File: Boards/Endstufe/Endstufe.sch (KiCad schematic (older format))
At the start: 56 parts, among them K1 DIP 7212-D, P1 CONN_3, P2 Trafo, P3 Relais, P4 6V3_AC, P5 Trafo_GK, P6 6V3_DC, P7 VSup1, P8 Bias, P9 CONN_5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

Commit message: Work in Progress
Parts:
- removed K1: DIP 7212-D, Reed:REED, symbol DIP~7212-D
- removed P1: CONN_3, MiniUniversalMate-N-LokSockets_13Aug2012:MiniUniversalMate-N-LokSocket_3PinVertical_12Aug2012, symbol CONN_3
- removed P3: Relais, w_conn_kk156:kk156_26-60-4020, symbol CONN_2
- removed P9: CONN_5, symbol CONN_5
- removed R24: 30k, Resistors_ThroughHole:Resistor_Horizontal_RM10mm, symbol R
- added J1: HV In, Connector_TE-Connectivity:TE_MATE-N-LOK_1-770875-x_2x03_P4.14mm_Vertical, symbol Endstufe-rescue:Conn_01x06
- added J2: Relais, Connector_Molex:Molex_KK-254_AE-6410-02A_1x02_P2.54mm_Vertical, symbol Endstufe-rescue:Conn_01x02
- added J3: NF_In, Connector_Molex:Molex_KK-254_AE-6410-02A_1x02_P2.54mm_Vertical, symbol Endstufe-rescue:Conn_01x02
- added K1: G6E, Relay_THT:Relay_SPDT_Omron_G6E, symbol Endstufe-rescue:G6E
- C1, C12, C13, C5: footprint Capacitors_ThroughHole:C_Disc_D7.5_P5 -> Capacitor_THT:C_Disc_D7.5mm_W4.4mm_P5.00mm; symbol C -> Endstufe-rescue:C
- C10, C11, C2, C3, C4, C8: footprint Capacitors_ThroughHole:C_Axial_D8_L21_P28 -> Capacitor_THT:C_Axial_L22.0mm_D9.5mm_P27.50mm_Horizontal; symbol C -> Endstufe-rescue:C
- C14, C15: footprint Capacitors_ThroughHole:C_Radial_D6.3_L11.2_P2.5 -> Capacitor_THT:CP_Radial_D6.3mm_P2.50mm; symbol C_Small -> Endstufe-rescue:C_Small
- C6: footprint Capacitors_ThroughHole:C_Disc_D6_P5 -> Capacitor_THT:C_Disc_D6.0mm_W2.5mm_P5.00mm; symbol C -> Endstufe-rescue:C
- C7: footprint Capacitors_ThroughHole:C_Disc_D3_P2.5 -> Capacitor_THT:C_Disc_D3.0mm_W2.0mm_P2.50mm; symbol C -> Endstufe-rescue:C
- C9: footprint Capacitors_ThroughHole:C_Disc_D7.5_P5 -> Capacitor_THT:C_Disc_D7.5mm_W2.5mm_P5.00mm; symbol C -> Endstufe-rescue:C
- P2: footprint Sockets_WAGO734:WAGO_734_5pin_Straight -> TerminalBlock_RND:TerminalBlock_RND_205-00004_1x05_P5.00mm_Horizontal; symbol CONN_5 -> Endstufe-rescue:CONN_5
- P4, P5, P6, P7: footprint Sockets_Mini-Universal:MiniUniversalMate-N-LokSocket_2PinVertical -> Connector_TE-Connectivity:TE_MATE-N-LOK_1-770866-x_1x02_P4.14mm_Vertical; symbol CONN_2 -> Endstufe-rescue:CONN_2
- P8: footprint Pin_Headers:Pin_Header_Straight_2x03_Pitch2.54mm -> Connector_PinHeader_2.54mm:PinHeader_2x03_P2.54mm_Vertical; symbol CONN_01X06 -> Endstufe-rescue:CONN_01X06
- R1, R11, R14, R15, R17, R18, R19, R2, R21, R22, R3, R6, R7, R8, R9: footprint Resistors_ThroughHole:Resistor_Horizontal_RM10mm -> Resistor_THT:R_Axial_DIN0207_L6.3mm_D2.5mm_P10.16mm_Horizontal; symbol R -> Endstufe-rescue:R
- R10, R13, R20, R23, R5: footprint Resistors_ThroughHole:Resistor_Ceramic_Horizontal_L23mm-W9mm-H9mm-p30mm -> Resistor_THT:R_Axial_Power_L25.0mm_W9.0mm_P30.48mm; symbol R -> Endstufe-rescue:R
- R12, R4: footprint Resistors_ThroughHole:Resistor_Horizontal_RM15mm -> Resistor_THT:R_Axial_DIN0207_L6.3mm_D2.5mm_P15.24mm_Horizontal; symbol R -> Endstufe-rescue:R
- R16: footprint Resistors_ThroughHole:Resistor_Horizontal_RM15mm -> Resistor_THT:R_Axial_DIN0207_L6.3mm_D2.5mm_P10.16mm_Horizontal; symbol R -> Endstufe-rescue:R
- RV2, RV3, RV5: footprint w_pth_resistors:trimmer_piher_pt10xv10 -> Potentiometer_THT:Potentiometer_Piher_PT-10-V10_Vertical; symbol POT-RESCUE-Endstufe -> Endstufe-rescue:POT-RESCUE-Endstufe
- T1, T2: footprint Valves:VALVE-OCTAL -> Valve:Valve_Octal; symbol KT88 -> Endstufe-rescue:KT88
- U1, U2: footprint Valves:VALVE-ECC-83-1 -> Valve:Valve_ECC-83-1; symbol ECC83 -> Endstufe-rescue:ECC83
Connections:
- net labels removed: 6V3
- wire segments 158 -> 205
- no-connect marks 0 -> 1

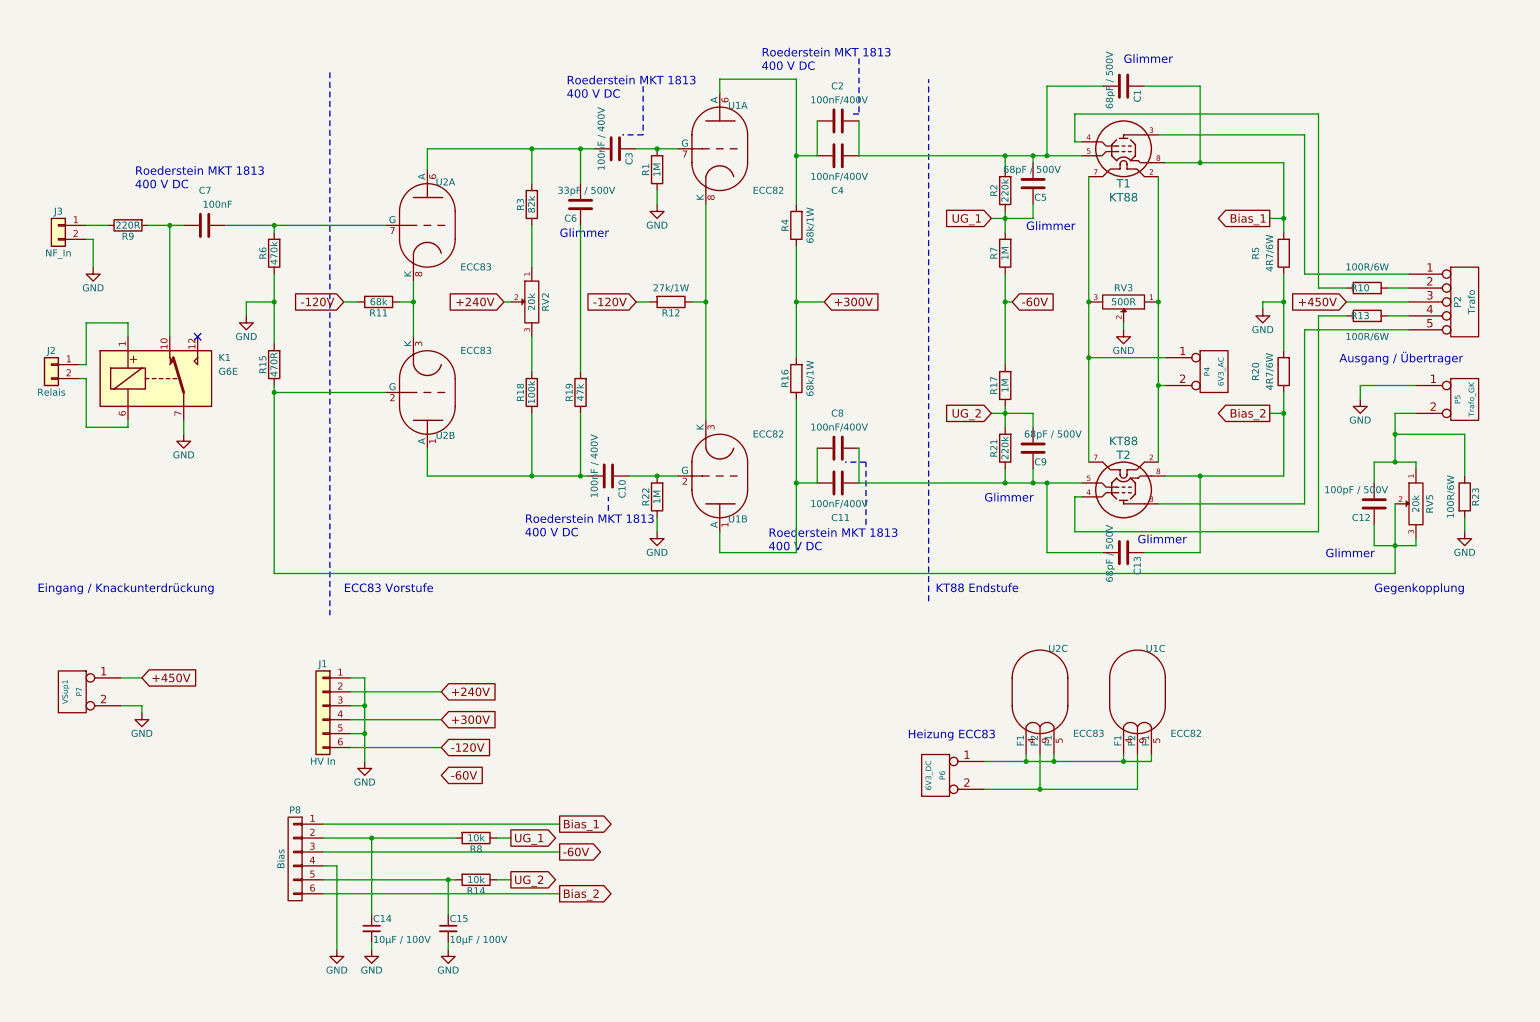
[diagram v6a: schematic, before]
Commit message: Converted to Kicad 5.1 and Layout changes
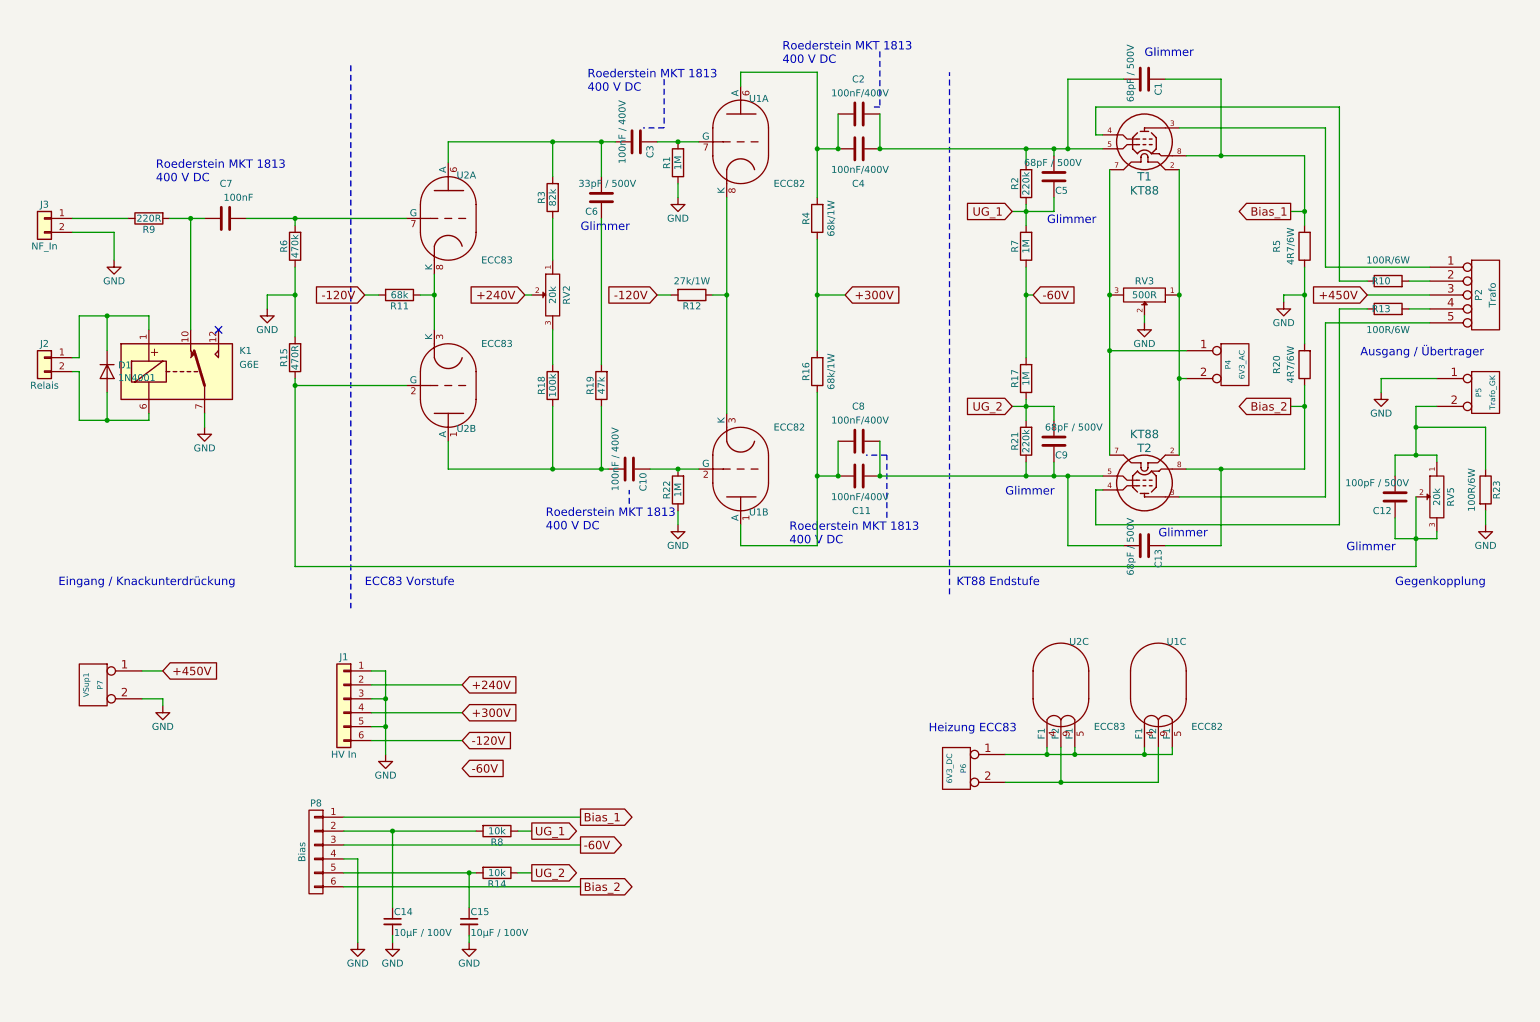
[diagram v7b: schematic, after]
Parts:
- added D1: 1N4001, Diode_THT:D_DO-41_SOD81_P10.16mm_Horizontal, symbol Diode:1N4001
- C14, C15: footprint Capacitor_THT:CP_Radial_D6.3mm_P2.50mm -> Capacitor_THT:C_Radial_D6.3mm_H5.0mm_P2.50mm
- R12: footprint Resistor_THT:R_Axial_DIN0207_L6.3mm_D2.5mm_P15.24mm_Horizontal -> Resistor_THT:R_Axial_DIN0414_L11.9mm_D4.5mm_P20.32mm_Horizontal
- R16: footprint Resistor_THT:R_Axial_DIN0207_L6.3mm_D2.5mm_P10.16mm_Horizontal -> Resistor_THT:R_Axial_DIN0414_L11.9mm_D4.5mm_P15.24mm_Horizontal
- R4: footprint Resistor_THT:R_Axial_DIN0207_L6.3mm_D2.5mm_P15.24mm_Horizontal -> Resistor_THT:R_Axial_DIN0414_L11.9mm_D4.5mm_P15.24mm_Horizontal
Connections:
- net at J2.1 (Pin_1), K1.1: now also D1.1 (K)
- net at J2.2 (Pin_2), K1.6: now also D1.2 (A)
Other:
- moved on the sheet: C1, C10, C11, C12, C13, C14, C15, C2, C3, C4, C5, C6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

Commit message: Layout changes after migrate to Kicad 5.1
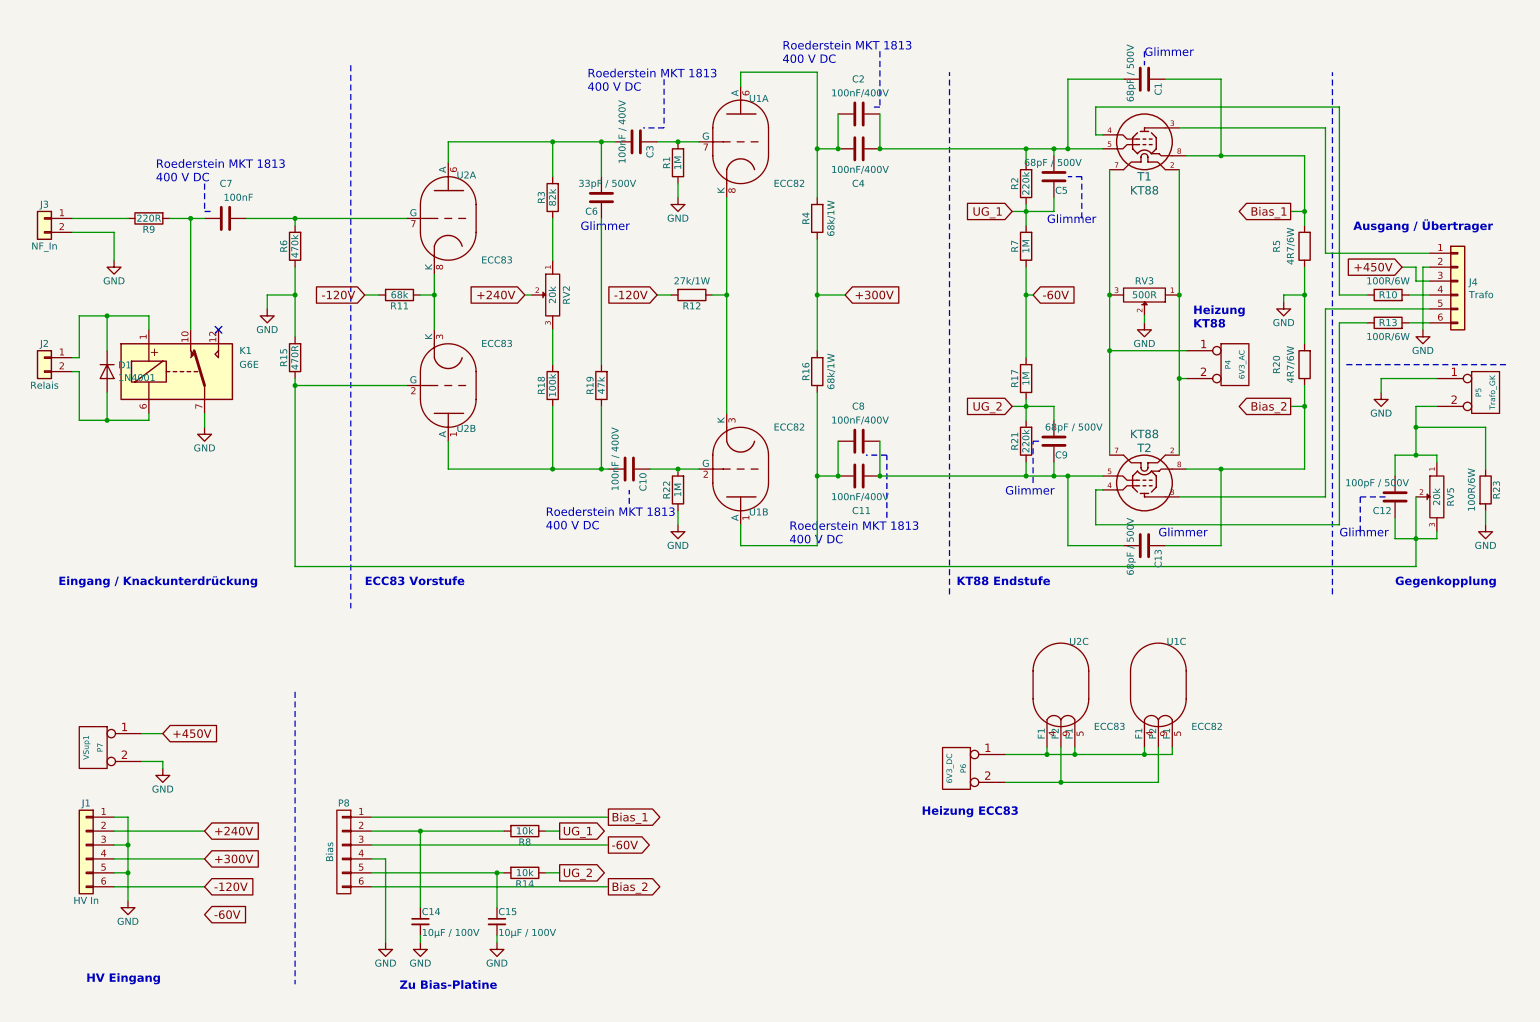
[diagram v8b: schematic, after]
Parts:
- removed P2: Trafo, TerminalBlock_RND:TerminalBlock_RND_205-00004_1x05_P5.00mm_Horizontal, symbol Endstufe-rescue:CONN_5
- added J4: Trafo, Connector_TE-Connectivity:TE_MATE-N-LOK_1-770875-x_2x03_P4.14mm_Vertical, symbol Connector_Generic:Conn_01x06
- J3: footprint Connector_Molex:Molex_KK-254_AE-6410-02A_1x02_P2.54mm_Vertical -> Connector_JST:JST_EH_B2B-EH-A_1x02_P2.50mm_Vertical
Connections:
- net +450V: now also J4.3 (Pin_3)
- net GND: now also J4.2 (Pin_2)
- net at T1.3 (a): now also J4.1 (Pin_1)
- net at T2.3 (a): now also J4.5 (Pin_5)
- net at R10.2: now also J4.4 (Pin_4)
- net at R13.2: now also J4.6 (Pin_6)
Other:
- note added: "HV Eingang"
- note added: "Heizung\nKT88"
- note added: "Zu Bias-Platine"
- moved on the sheet: C14, C15, J1, P7, P8, R10, R13, R14, R8
